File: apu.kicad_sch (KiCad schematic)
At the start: 1 part, among them J1 Conn_02x07_Top_Bottom

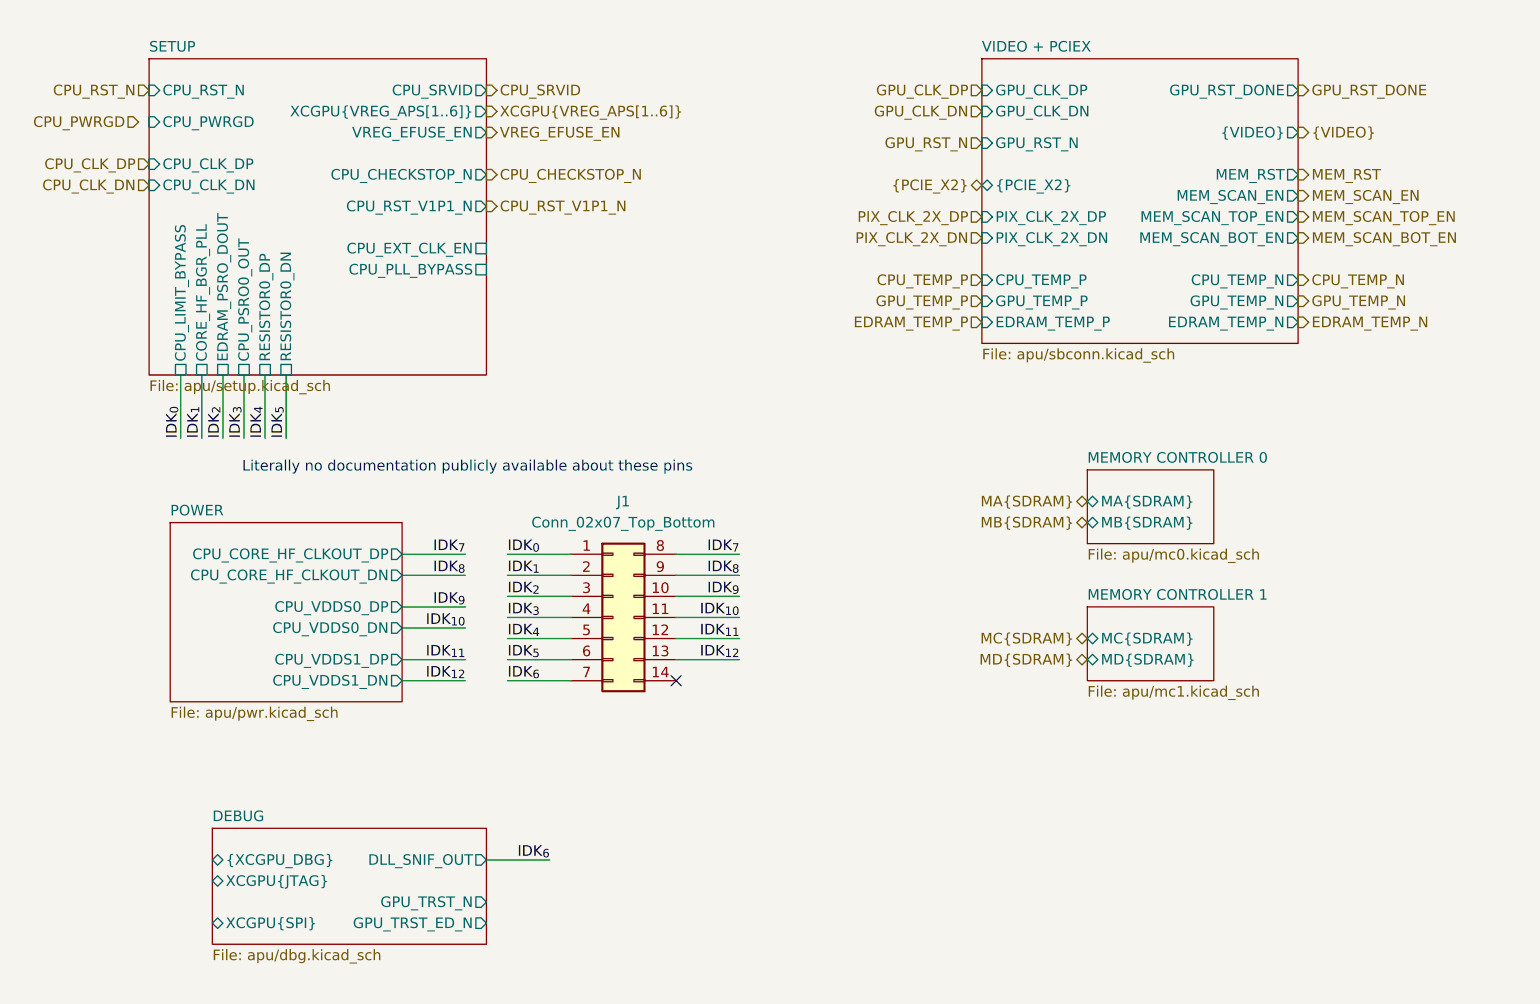
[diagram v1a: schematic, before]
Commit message: Cleanup, SMC GPIO connections and Temperature sensing
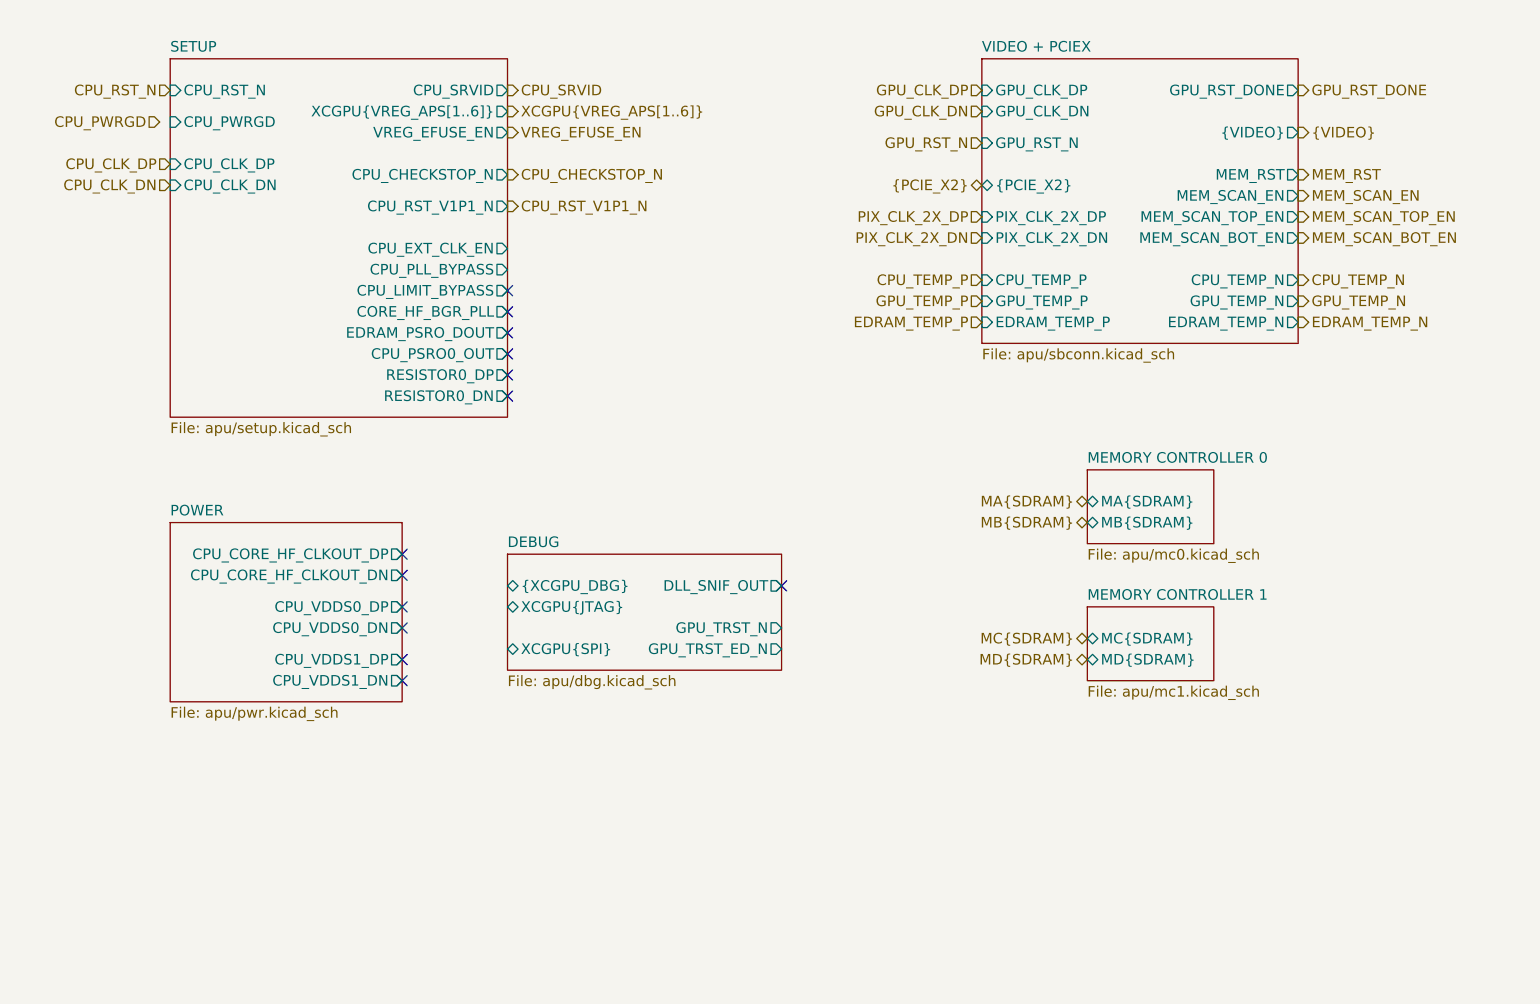
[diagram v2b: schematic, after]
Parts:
- removed J1: Conn_02x07_Top_Bottom, symbol Connector_Generic:Conn_02x07_Top_Bottom
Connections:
- no-connect marks 1 -> 13
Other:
- note removed: "Literally no documentation publicly available about these pins"

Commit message: Cleanup & Debug I/O
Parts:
- added J3: Conn_01x02, symbol Connector_Generic:Conn_01x02
- added J4: Conn_02x03_Odd_Even, symbol Connector_Generic:Conn_02x03_Odd_Even
- added J5: Conn_02x04_Odd_Even, symbol Connector_Generic:Conn_02x04_Odd_Even
- added J6: Conn_02x12_Top_Bottom, symbol Connector_Generic:Conn_02x12_Top_Bottom
- added TP25, TP26, TP27, TP28, TP29, TP30, TP31, TP32, TP33, TP34, TP35, TP36, TP37: TestPoint_Small, symbol Connector:TestPoint_Small
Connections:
- net DEBUG/DLL_SNIF_OUT: now also TP37.1
- net POWER/CPU_CORE_HF_CLKOUT_DN: now also TP32.1
- net POWER/CPU_CORE_HF_CLKOUT_DP: now also TP31.1
- net POWER/CPU_VDDS0_DN: now also TP34.1
- net POWER/CPU_VDDS0_DP: now also TP33.1
- net POWER/CPU_VDDS1_DN: now also TP36.1
- net POWER/CPU_VDDS1_DP: now also TP35.1
- net SETUP/CORE_HF_BGR_PLL: now also TP26.1
- net SETUP/CPU_EXT_CLK_EN: now also J3.2 (Pin_2)
- net SETUP/CPU_LIMIT_BYPASS: now also TP25.1
- net SETUP/CPU_PLL_BYPASS: now also J3.1 (Pin_1)
- net SETUP/CPU_PSRO0_OUT: now also TP28.1
- net SETUP/EDRAM_PSRO_DOUT: now also TP27.1
- net SETUP/RESISTOR0_DN: now also TP30.1
- net SETUP/RESISTOR0_DP: now also TP29.1
- new net CPUCLK0: J6.7 (Pin_7)
- new net CPUCLK1: J6.8 (Pin_8)
- new net GND: J4.6 (Pin_6), J5.6 (Pin_6), J6.24 (Pin_24)
- new net GPUCLK0: J6.9 (Pin_9)
- new net GPUCLK1: J6.10 (Pin_10)
- new net GPU_HB: J6.6 (Pin_6)
- new net GPU_TRST_ED_N: J5.8 (Pin_8)
- new net GPU_TRST_N: J5.4 (Pin_4)
- new net POST_IN0: J6.1 (Pin_1)
- new net POST_IN1: J6.2 (Pin_2)
- new net POST_IN2: J6.3 (Pin_3)
- new net POST_IN3: J6.4 (Pin_4)
- new net POST_IN4: J6.5 (Pin_5)
- new net POST_OUT0: J6.13 (Pin_13)
- new net POST_OUT1: J6.14 (Pin_14)
- new net POST_OUT2: J6.15 (Pin_15)
- new net POST_OUT3: J6.16 (Pin_16)
- new net POST_OUT4: J6.17 (Pin_17)
- new net POST_OUT5: J6.18 (Pin_18)
- new net POST_OUT6: J6.19 (Pin_19)
- new net POST_OUT7: J6.20 (Pin_20)
- new net RESET0: J6.21 (Pin_21)
- new net RESET1: J6.22 (Pin_22)
- new net RESET2: J6.23 (Pin_23)
- new net TBCLK0: J6.11 (Pin_11)
- new net TBCLK1: J6.12 (Pin_12)
- new net XCGPU.CLK: J4.1 (Pin_1)
- new net XCGPU.CS: J4.5 (Pin_5)
- new net XCGPU.MISO: J4.2 (Pin_2)
- new net XCGPU.MOSI: J4.3 (Pin_3)
- new net XCGPU.TCK: J5.5 (Pin_5)
- new net XCGPU.TDI: J5.1 (Pin_1)
- new net XCGPU.TDO: J5.3 (Pin_3)
- new net XCGPU.TMS: J5.2 (Pin_2)
- new net XCGPU.TRST: J5.7 (Pin_7)
- new net XCGPU.WP: J4.4 (Pin_4)
- no-connect marks 13 -> 0
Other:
- note added: "I'm so tired"

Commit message: Debug Connectors
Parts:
- removed J4: Conn_02x03_Odd_Even, symbol Connector_Generic:Conn_02x03_Odd_Even
- removed J5: Conn_02x04_Odd_Even, symbol Connector_Generic:Conn_02x04_Odd_Even
- removed J6: Conn_02x12_Top_Bottom, symbol Connector_Generic:Conn_02x12_Top_Bottom
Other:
- note removed: "I'm so tired"
- moved on the sheet: J3, TP25, TP26, TP27, TP28, TP29, TP30, TP31, TP32, TP33, TP34, TP35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

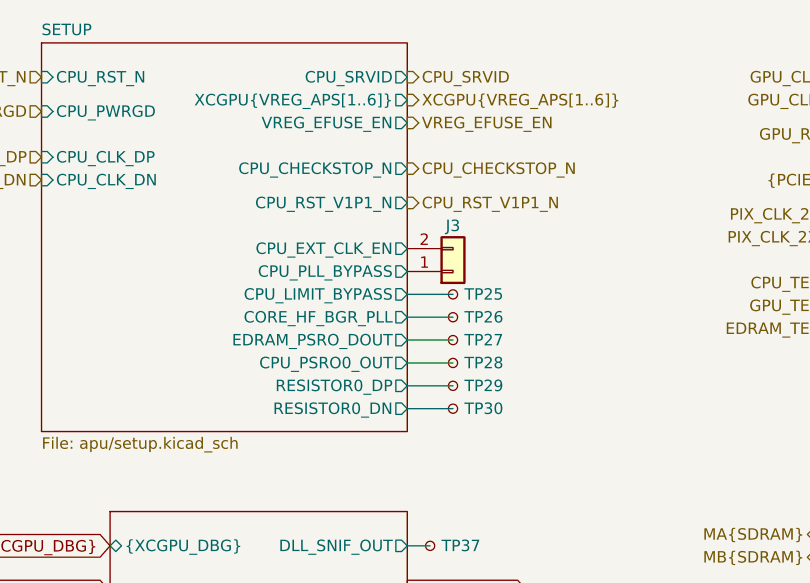
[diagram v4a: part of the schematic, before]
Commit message: Nand Flash, Sata Connectors and removing (hopefully) unnecessary things
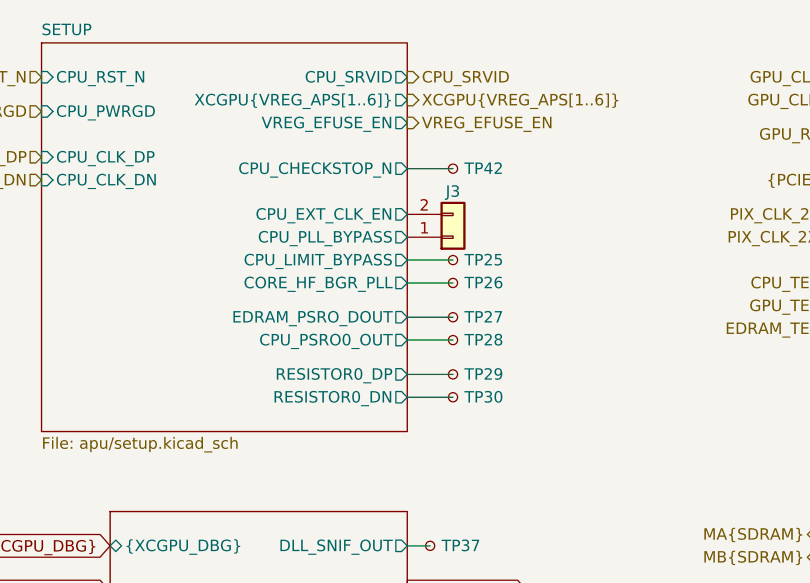
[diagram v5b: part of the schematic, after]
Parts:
- added TP42: TestPoint_Small, symbol Connector:TestPoint_Small
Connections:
- new net SETUP/CPU_CHECKSTOP_N: TP42.1
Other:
- sheet SETUP ports: added none; removed CPU_RST_V1P1_N
- moved on the sheet: J3, TP25, TP26, TP27, TP28, TP29, TP30
